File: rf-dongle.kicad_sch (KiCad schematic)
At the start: 38 parts, among them J1 USB_A, SW1 SW_Push, U1 NRF52840-QIAA-R7, X1 32MHz, X2 32.768kHz

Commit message: reverse USB pads and remove unnecessary component
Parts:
- removed R2: 10k, Resistor_SMD:R_0402_1005Metric_Pad0.72x0.64mm_HandSolder, symbol Device:R
- removed SW1: SW_Push, Button_Switch_SMD:SW_SPST_B3U-1000P, symbol Switch:SW_Push
- C9: now not fitted; now left out of the parts list
- J1: now in the parts list
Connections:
- net RESET: no longer names the net of U1.AC13 (~{RESET})
- no-connect marks 46 -> 48
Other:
- note added: "BOM: - nRF52840 QIAA (aQFN), NRF52840-QIAA-R7 - Crystal 32MHz 8pF 2.0x1.6mm, CX2016SA32000D0WRQG1 - Crystal 32.768kHz 2.0x1.2mm, ABS06N-32.768kHz-9-T - Chip ant 2.4GHz 0.5dBi, 2450AT18A100E - 5v ESD protection TVS diode, PRTR5V0U2X-HXY - Inductor 4.7nH 5% - Res. 0402 2R2 1% - Res. 0402 56 1% - Cap. 12pF C0G 0402 2% - Cap. 100nF X7R 10% - Cap. 4.7uF X7R 0603 - Cap. 0.8pF C0G 0.05% - Cap. 0.5pF C0G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"
- note added: "C9 not required for Fxx and later"
- note added: "Most of the schematic is a direct copy of the reference schematic for the QIAA layout. The only exceptions are the LEDs and programming pins."
- note added: "The antenna should have its own matching network, used to tune the antenna's frequency, omitting it for now, since I have no way to tune the components after the PCB is produced."
- note removed: "BOM: - nRF52840 QIAA (aQFN), NRF52840-QIAA-R7, 3.3474 EUR - 5v ESD protection, PRTR5V0U2X-HXY, 0.0371 EUR ? Cap. 50v 12pF C0G 1%, GJM1555C1H120FB01D, 0.0293 EUR ? Cap. 50v 100nF X7R 10%, GRM155R71H104KE14D, 0.0026 EUR ? Cap. 25v 10nF X7R 10%, GRM155R71E103KA01D, 0.0014 EUR ? Res. 62.5mW 2R2 1%, 0402WGF220KTCE, 0.0007 EUR ? Res. 62.5mW 10k 1%, 0402WGF1002TCE, 0.0004 EUR - LED 20mA 35mcd 2V Yel., B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"
- note removed: "Most of the schematic is a direct copy of the reference schematic for the QFAA layout. The only exceptions are the LEDs, programming pins and reset button."
- note removed: "Reset Button"
- note removed: "Reset pin can technically be configured to either reset on connect or disconnect, but it's pulled up on nRF52-DK and Dongle, so pulling it up here as well."
- note removed: "Resistor and decoupling capacitor values are copied from the nRF52-Dongle schematic."
- note removed: "The antenna should have its own matching network, used to tune the antenna's frequency, omitting it for now, since I have no way to tune such the components after the PCB is produced."
- moved on the sheet: D2, D3, H1, H2, H3, H4, H5, R3, R4

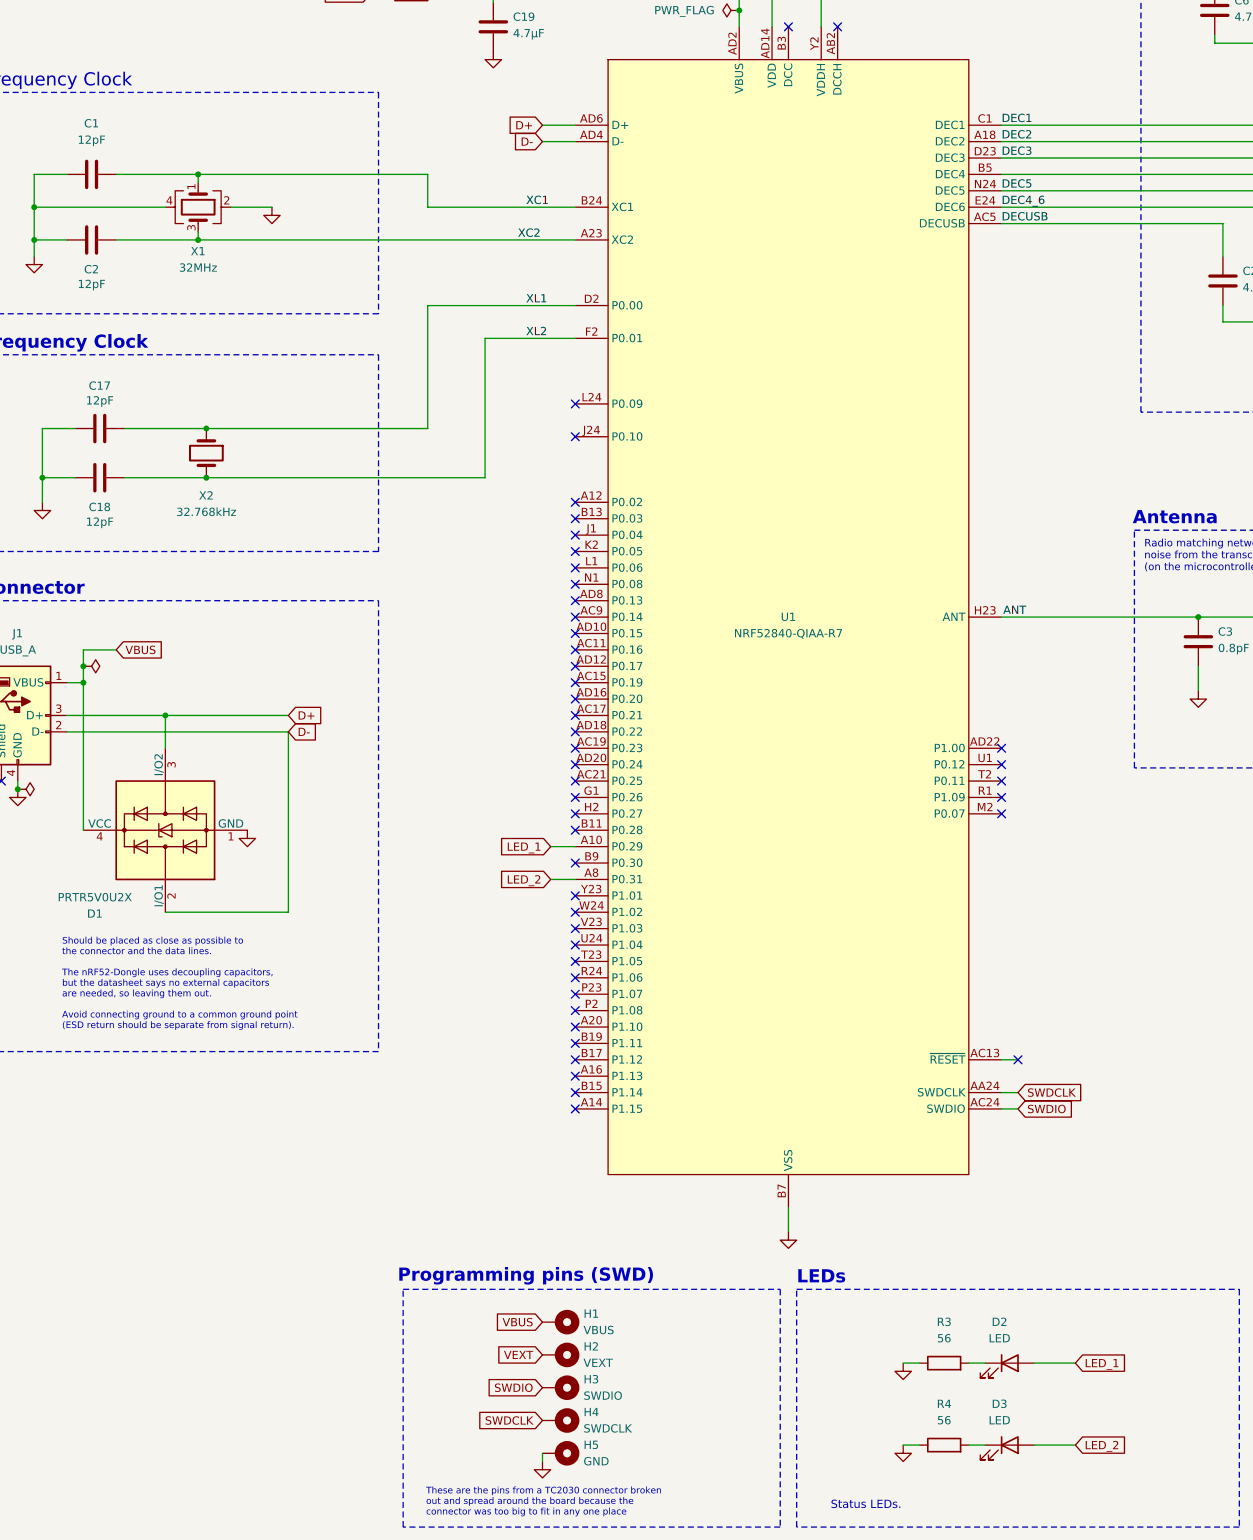
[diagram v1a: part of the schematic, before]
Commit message: ordered rev 3
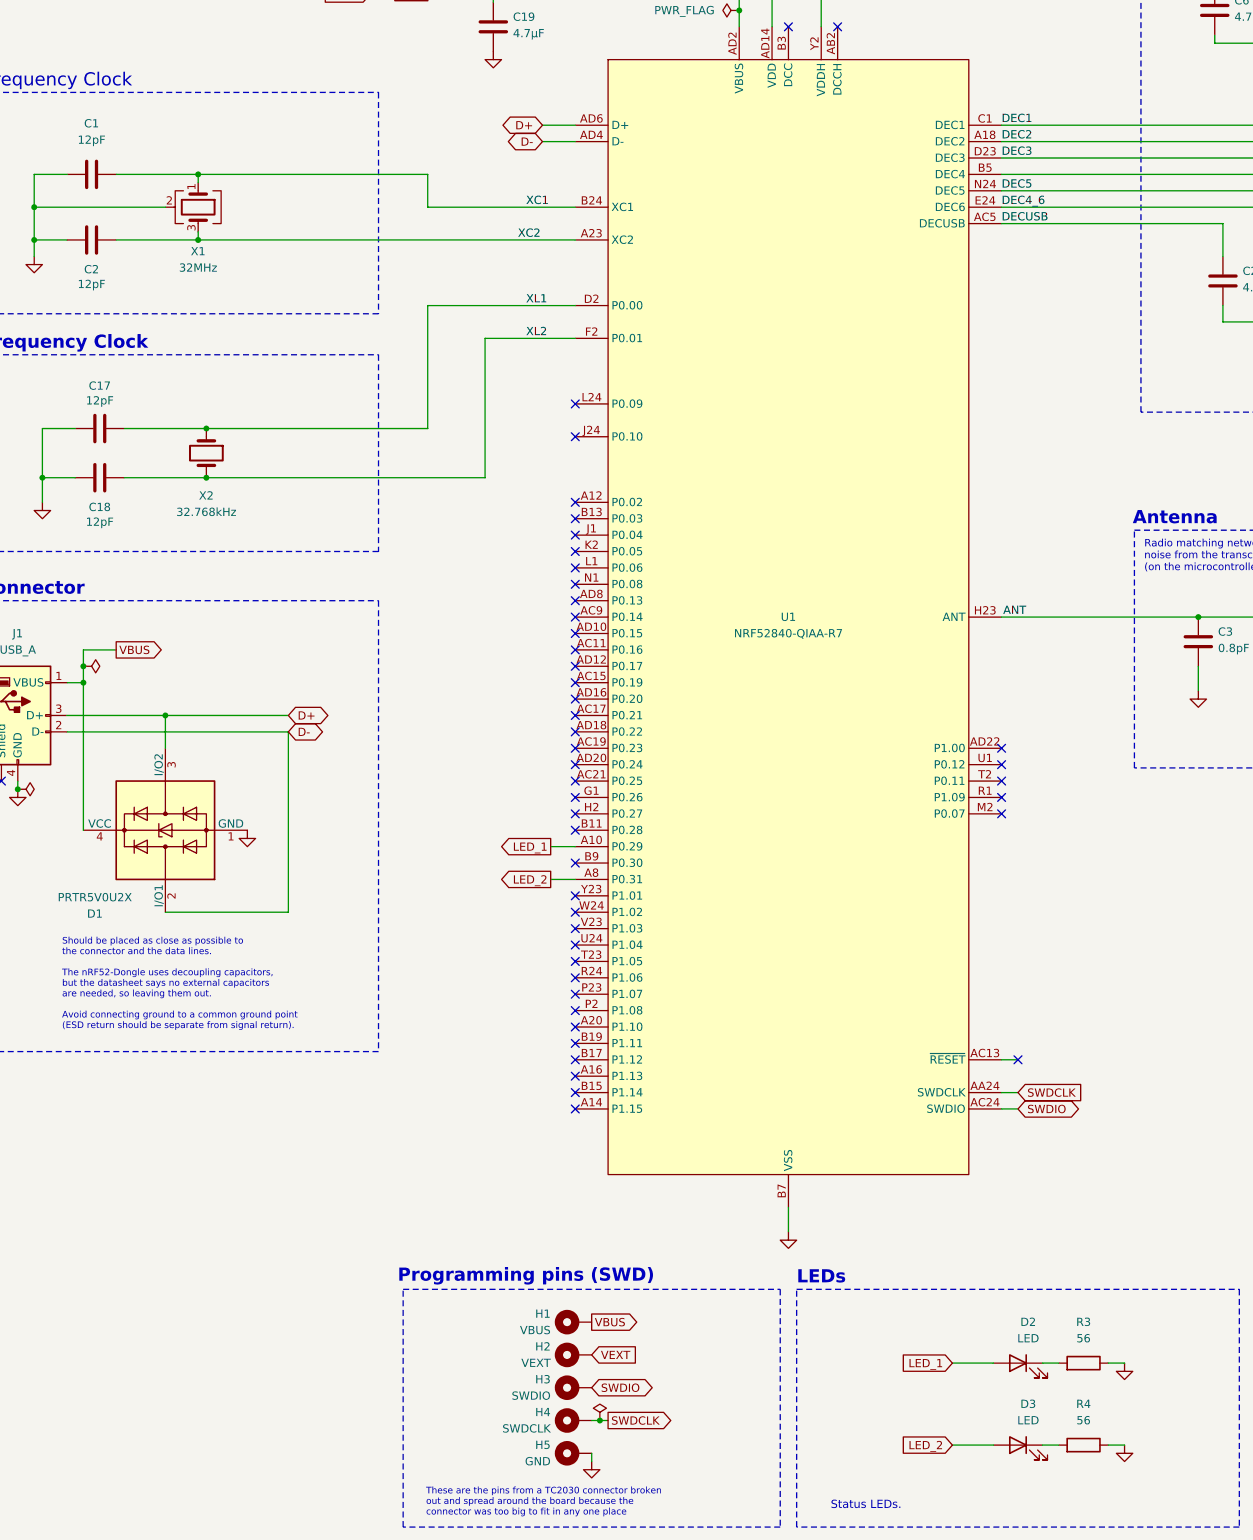
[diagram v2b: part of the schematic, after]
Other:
- moved on the sheet: D2, D3, H1, H2, H3, H4, H5, R3, R4
